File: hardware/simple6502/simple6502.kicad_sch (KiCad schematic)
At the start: 20 parts, among them J1 ~{VP}, J2 CLK SEL, J3 RESET, J4 6502 BUS, SW1 RESET, T1 DS1813-10+, U1 W65C02SxP, U2 CY62256-70PC, U3 28C256, U4 74LS30, U5 74HCT00, X1 ACO-1MHz

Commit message: Footprint round 1
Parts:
- J1, J3: footprint (none) -> Connector_PinHeader_2.54mm:PinHeader_1x02_P2.54mm_Vertical
- J2: footprint (none) -> Connector_PinHeader_2.54mm:PinHeader_1x03_P2.54mm_Vertical
- R1, R2, R3, R4, R5: footprint (none) -> Resistor_THT:R_Axial_DIN0204_L3.6mm_D1.6mm_P7.62mm_Horizontal
- SW1: footprint (none) -> Button_Switch_THT:SW_TH_Tactile_Omron_B3F-10xx
- TP1, TP2, TP3: footprint (none) -> TestPoint:TestPoint_THTPad_3.0x3.0mm_Drill1.5mm
- U3: footprint (none) -> Package_DIP:DIP-28_W15.24mm_Socket
- U4, U5: footprint (none) -> Package_DIP:DIP-14_W7.62mm_Socket
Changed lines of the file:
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@@
       (effects (font (size 1.27 1.27)))
     )
-    (property "Footprint" "" (at 252.73 99.06 0)
+    (property "Footprint" "Connector_PinHeader_2.54mm:PinHeader_1x03_P2.54mm_Vertical" (at 252.73 99.06 0)
       (effects (font (size 1.27 1.27)) hide)
     )
@@
       (effects (font (size 1.27 1.27)))
     )
-    (property "Footprint" "" (at 40.64 57.912 90)
+    (property "Footprint" "Resistor_THT:R_Axial_DIN0204_L3.6mm_D1.6mm_P7.62mm_Horizontal" (at 40.64 57.912 90)
       (effects (font (size 1.27 1.27)) hide)
     )
@@
       (effects (font (size 1.27 1.27)))
     )
-    (property "Footprint" "" (at 142.24 93.98 0)
+    (property "Footprint" "Package_DIP:DIP-14_W7.62mm_Socket" (at 142.24 93.98 0)
       (effects (font (size 1.27 1.27)) hide)
     )
@@
       (effects (font (size 1.27 1.27)) (justify right))
     )
-    (property "Footprint" "" (at 217.17 154.94 0)
+    (property "Footprint" "Button_Switch_THT:SW_TH_Tactile_Omron_B3F-10xx" (at 217.17 154.94 0)
       (effects (font (size 1.27 1.27)) hide)
     )
@@
       (effects (font (size 1.27 1.27)))
     )
-    (property "Footprint" "" (at 28.448 35.56 90)
+    (property "Footprint" "Resistor_THT:R_Axial_DIN0204_L3.6mm_D1.6mm_P7.62mm_Horizontal" (at 28.448 35.56 90)
       (effects (font (size 1.27 1.27)) hide)
     )
@@
       (effects (font (size 1.27 1.27)))
     )
-    (property "Footprint" "" (at 124.46 111.76 0)
+    (property "Footprint" "Package_DIP:DIP-14_W7.62mm_Socket" (at 124.46 111.76 0)
       (effects (font (size 1.27 1.27)) hide)
     )
@@
       (effects (font (size 1.27 1.27)))
     )
-    (property "Footprint" "" (at 252.73 168.91 0)
+    (property "Footprint" "TestPoint:TestPoint_THTPad_3.0x3.0mm_Drill1.5mm" (at 252.73 168.91 0)
       (effects (font (size 1.27 1.27)) hide)
     )
@@
       (effects (font (size 1.27 1.27)) (justify left))
     )
-    (property "Footprint" "" (at 218.44 54.61 0)
+    (property "Footprint" "Package_DIP:DIP-28_W15.24mm_Socket" (at 218.44 54.61 0)
       (effects (font (size 1.27 1.27)) hide)
     )
@@
       (effects (font (size 1.27 1.27)))
     )
-    (property "Footprint" "" (at 204.47 168.91 0)
+    (property "Footprint" "TestPoint:TestPoint_THTPad_3.0x3.0mm_Drill1.5mm" (at 204.47 168.91 0)
       (effects (font (size 1.27 1.27)) hide)
     )
@@
       (effects (font (size 1.27 1.27)))
     )
-    (property "Footprint" "" (at 186.69 168.91 0)
+    (property "Footprint" "TestPoint:TestPoint_THTPad_3.0x3.0mm_Drill1.5mm" (at 186.69 168.91 0)
       (effects (font (size 1.27 1.27)) hide)
     )
@@
       (effects (font (size 1.27 1.27)))
     )
-    (property "Footprint" "" (at 33.02 58.928 90)
+    (property "Footprint" "Resistor_THT:R_Axial_DIN0204_L3.6mm_D1.6mm_P7.62mm_Horizontal" (at 33.02 58.928 90)
       (effects (font (size 1.27 1.27)) hide)
     )
@@
       (effects (font (size 1.27 1.27)) (justify left))
     )
-    (property "Footprint" "" (at 232.41 154.94 0)
+    (property "Footprint" "Connector_PinHeader_2.54mm:PinHeader_1x02_P2.54mm_Vertical" (at 232.41 154.94 0)
       (effects (font (size 1.27 1.27)) hide)
     )
@@
       (effects (font (size 1.27 1.27)))
     )
-    (property "Footprint" "" (at 124.46 137.16 0)
+    (property "Footprint" "Package_DIP:DIP-14_W7.62mm_Socket" (at 124.46 137.16 0)
       (effects (font (size 1.27 1.27)) hide)
     )
@@
       (effects (font (size 1.27 1.27)))
     )
-    (property "Footprint" "" (at 16.51 69.85 0)
+    (property "Footprint" "Connector_PinHeader_2.54mm:PinHeader_1x02_P2.54mm_Vertical" (at 16.51 69.85 0)
       (effects (font (size 1.27 1.27)) hide)
     )
@@
       (effects (font (size 1.27 1.27)))
     )
-    (property "Footprint" "" (at 34.798 35.56 90)
+    (property "Footprint" "Resistor_THT:R_Axial_DIN0204_L3.6mm_D1.6mm_P7.62mm_Horizontal" (at 34.798 35.56 90)
       (effects (font (size 1.27 1.27)) hide)
     )
@@
       (effects (font (size 1.27 1.27)))
     )
-    (property "Footprint" "" (at 147.32 144.78 0)
+    (property "Footprint" "Package_DIP:DIP-14_W7.62mm_Socket" (at 147.32 144.78 0)
       (effects (font (size 1.27 1.27)) hide)
     )
@@
       (effects (font (size 1.27 1.27)))
     )
-    (property "Footprint" "" (at 160.02 109.22 0)
+    (property "Footprint" "Package_DIP:DIP-14_W7.62mm_Socket" (at 160.02 109.22 0)
       (effects (font (size 1.27 1.27)) hide)
     )
@@
       (effects (font (size 1.27 1.27)))
     )
-    (property "Footprint" "" (at 40.64 73.152 90)
-      (effects (font (size 1.27 1.27)) hide)
-    )
+    (property "Footprint" "Resistor_THT:R_Axial_DIN0204_L3.6mm_D1.6mm_P7.62mm_Horizontal" (at 40.64 73.152 90)
+      (effects (font (size 1.27 1.27)) hide)
+    )

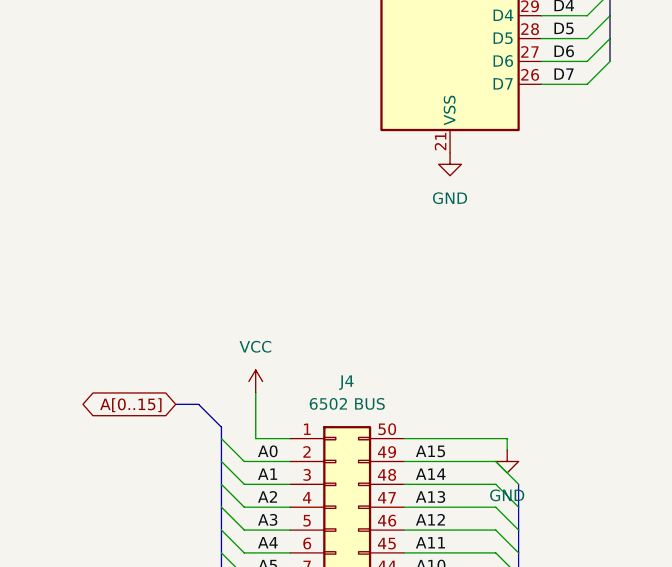
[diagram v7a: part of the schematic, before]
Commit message: Added Apple II connector footprint and 3d model
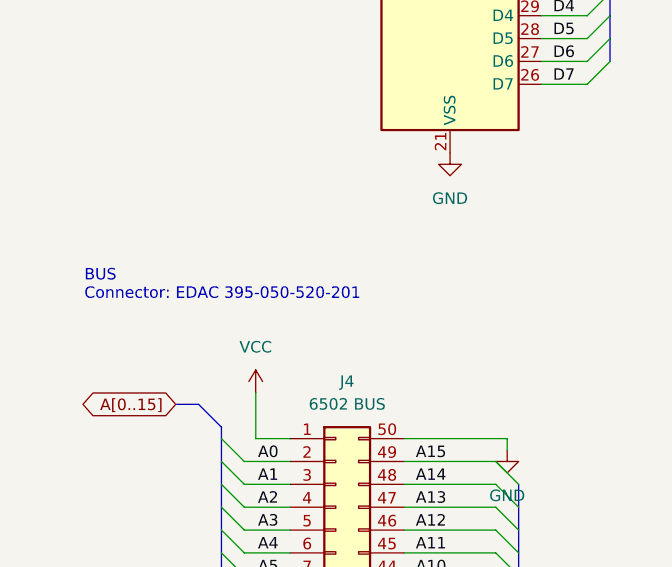
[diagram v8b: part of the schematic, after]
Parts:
- J4: footprint (none) -> Connector_Card:EDAC 395-050-520-201
- T1: footprint DS1813-10+:21-0248A -> DS1813-10_:21-0248A
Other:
- note added: "BUS Connector: EDAC 395-050-520-201"
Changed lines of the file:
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@@
+    (effects (font (size 1.27 1.27)) (justify left bottom))
+  )
+  (text "BUS\nConnector: EDAC 395-050-520-201" (at 19.05 114.3 0)
     (effects (font (size 1.27 1.27)) (justify left bottom))
   )
@@
       (effects (font (size 1.27 1.27)))
     )
-    (property "Footprint" "DS1813-10+:21-0248A" (at 224.79 156.21 0)
+    (property "Footprint" "DS1813-10_:21-0248A" (at 224.79 156.21 0)
       (effects (font (size 1.27 1.27)) (justify bottom) hide)
     )
@@
       (effects (font (size 1.27 1.27)))
     )
-    (property "Footprint" "" (at 46.99 160.02 0)
-      (effects (font (size 1.27 1.27)) hide)
-    )
+    (property "Footprint" "Connector_Card:EDAC 395-050-520-201" (at 46.99 160.02 0)
+      (effects (font (size 1.27 1.27)) hide)
+    )
